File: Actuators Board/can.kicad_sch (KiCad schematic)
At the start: 14 parts, among them U4 SN65HVD230

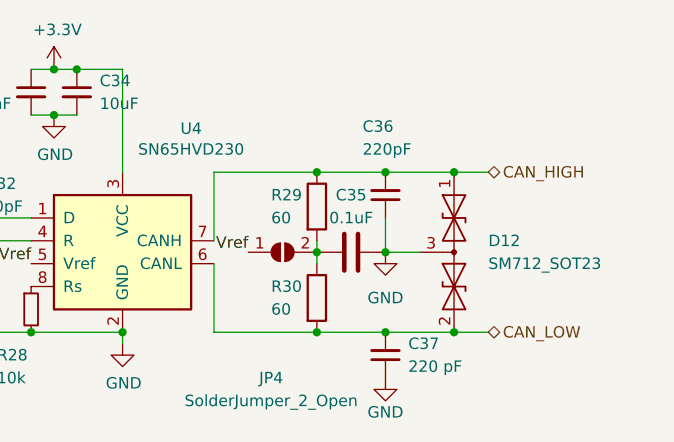
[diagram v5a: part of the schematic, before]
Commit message: Added CAN transceiver and new connector to board
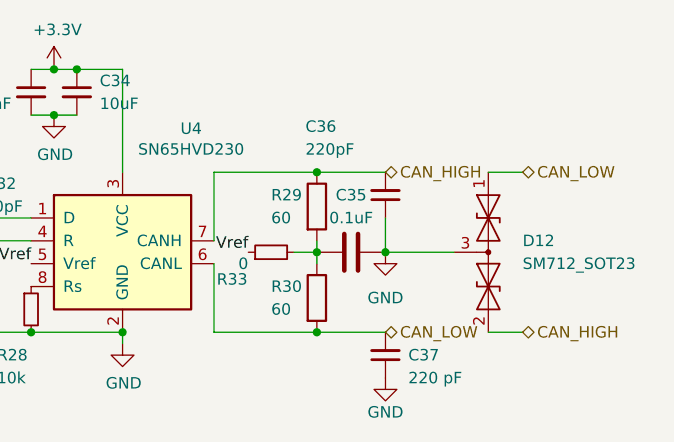
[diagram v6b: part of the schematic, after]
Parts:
- removed JP4: SolderJumper_2_Open, Jumper:SolderJumper-2_P1.3mm_Open_Pad1.0x1.5mm, symbol Jumper:SolderJumper_2_Open
- added R33: 0, Resistor_SMD:R_0603_1608Metric, symbol Device:R_Small
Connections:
- net CAN_HIGH: now also D12.2 (A2); no longer D12.1 (A1)
- net CAN_LOW: now also D12.1 (A1); no longer D12.2 (A2)
- net Vref: now also R33.1
- net at C35.1, R29.2, R30.1: now also R33.2
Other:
- moved on the sheet: D12
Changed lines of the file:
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@@
   (junction (at 163.83 88.9) (diameter 0) (color 0 0 0 0)
   )
-  (junction (at 163.83 97.79) (diameter 0) (color 0 0 0 0)
-  )
   (junction (at 124.46 97.79) (diameter 0) (color 0 0 0 0)
   )
-  (junction (at 171.45 80.01) (diameter 0) (color 0 0 0 0)
-  )
   (junction (at 156.21 97.79) (diameter 0) (color 0 0 0 0)
   )
@@
   (junction (at 134.62 97.79) (diameter 0) (color 0 0 0 0)
   )
-  (junction (at 171.45 97.79) (diameter 0) (color 0 0 0 0)
-  )
-  (junction (at 163.83 80.01) (diameter 0) (color 0 0 0 0)
-  )
   (junction (at 127 73.66) (diameter 0) (color 0 0 0 0)
   )
-  (wire (pts (xy 171.45 97.79) (xy 175.26 97.79))
+  (wire (pts (xy 175.26 97.79) (xy 179.07 97.79))
     (stroke (width 0) (type default) (color 0 0 0 0))
   )
@@
     (stroke (width 0) (type default) (color 0 0 0 0))
   )
-  (wire (pts (xy 163.83 88.9) (xy 167.64 88.9))
+  (wire (pts (xy 163.83 88.9) (xy 171.45 88.9))
     (stroke (width 0) (type default) (color 0 0 0 0))
   )
@@
     (stroke (width 0) (type default) (color 0 0 0 0))
   )
-  (wire (pts (xy 163.83 80.01) (xy 171.45 80.01))
-    (stroke (width 0) (type default) (color 0 0 0 0))
-  )
   (wire (pts (xy 156.21 97.79) (xy 163.83 97.79))
     (stroke (width 0) (type default) (color 0 0 0 0))
@@
     (stroke (width 0) (type default) (color 0 0 0 0))
   )
-  (wire (pts (xy 171.45 80.01) (xy 175.26 80.01))
+  (wire (pts (xy 175.26 80.01) (xy 179.07 80.01))
     (stroke (width 0) (type default) (color 0 0 0 0))
   )
@@
     (stroke (width 0) (type default) (color 0 0 0 0))
   )
-  (wire (pts (xy 163.83 97.79) (xy 171.45 97.79))
-    (stroke (width 0) (type default) (color 0 0 0 0))
-  )
   (wire (pts (xy 134.62 99.06) (xy 134.62 97.79))
     (stroke (width 0) (type default) (color 0 0 0 0))
@@
   )
   (wire (pts (xy 144.78 87.63) (xy 144.78 80.01))
+    (stroke (width 0) (type default) (color 0 0 0 0))
+  )
+  (wire (pts (xy 153.67 88.9) (xy 156.21 88.9))
     (stroke (width 0) (type default) (color 0 0 0 0))
   )
@@
     (effects (font (size 1.27 1.27)) (justify right bottom))
   )
-  (hierarchical_label "CAN_LOW" (shape bidirectional) (at 175.26 97.79 0)
-    (effects (font (size 1.27 1.27)) (justify left))
-  )
   (hierarchical_label "CAN_RX" (shape input) (at 111.76 87.63 180)
     (effects (font (size 1.27 1.27)) (justify right))
   )
+  (hierarchical_label "CAN_HIGH" (shape bidirectional) (at 163.83 80.01 0)
+    (effects (font (size 1.27 1.27)) (justify left))
+  )
   (hierarchical_label "CAN_TX" (shape output) (at 111.76 85.09 180)
     (effects (font (size 1.27 1.27)) (justify right))
   )
-  (hierarchical_label "CAN_HIGH" (shape bidirectional) (at 175.26 80.01 0)
+  (hierarchical_label "CAN_HIGH" (shape bidirectional) (at 179.07 97.79 0)
+    (effects (font (size 1.27 1.27)) (justify left))
+  )
+  (hierarchical_label "CAN_LOW" (shape bidirectional) (at 179.07 80.01 0)
+    (effects (font (size 1.27 1.27)) (justify left))
+  )
+  (hierarchical_label "CAN_LOW" (shape bidirectional) (at 163.83 97.79 0)
     (effects (font (size 1.27 1.27)) (justify left))
   )
@@
     (pin "2")
   )
-  (symbol (lib_id "Jumper:SolderJumper_2_Open") (at 152.4 88.9 0) (unit 1)
-    (in_bom yes) (on_board yes)
-    (property "Reference" "JP4" (id 0) (at 151.13 102.87 0))
-    (property "Value" "SolderJumper_2_Open" (id 1) (at 151.13 105.41 0))
-    (property "Footprint" "Jumper:SolderJumper-2_P1.3mm_Open_Pad1.0x1.5mm" (id 2) (at 152.4 88.9 0)
-      (effects (font (size 1.27 1.27)) hide)
-    )
-    (property "Datasheet" "~" (id 3) (at 152.4 88.9 0)
-      (effects (font (size 1.27 1.27)) hide)
-    )
-    (pin "1")
-    (pin "2")
-  )
   (symbol (lib_id "Device:C_Small") (at 163.83 82.55 180) (unit 1)
     (in_bom yes) (on_board yes)
-    (property "Reference" "C36" (id 0) (at 161.29 74.93 0)
-      (effects (font (size 1.27 1.27)) (justify right))
-    )
-    (property "Value" "220pF" (id 1) (at 161.29 77.47 0)
+    (property "Reference" "C36" (id 0) (at 154.94 74.93 0)
+      (effects (font (size 1.27 1.27)) (justify right))
+    )
+    (property "Value" "220pF" (id 1) (at 154.94 77.47 0)
       (effects (font (size 1.27 1.27)) (justify right))
     )
@@
     (pin "2")
   )
-  (symbol (lib_id "Diode:SM712_SOT23") (at 171.45 88.9 270) (unit 1)
-    (in_bom yes) (on_board yes)
-    (property "Reference" "D12" (id 0) (at 175.26 87.63 90)
-      (effects (font (size 1.27 1.27)) (justify left))
-    )
-    (property "Value" "SM712_SOT23" (id 1) (at 175.26 90.17 90)
-      (effects (font (size 1.27 1.27)) (justify left))
-    )
-    (property "Footprint" "Package_TO_SOT_SMD:SOT-23" (id 2) (at 162.56 88.9 0)
-      (effects (font (size 1.27 1.27)) hide)
-    )
-    (property "Datasheet" "https://www.littelfuse.com/~/media/electronics/datasheets/tvs_diode_arrays/littelfuse_tvs_diode_array_sm712_datasheet.pdf.pdf" (id 3) (at 171.45 85.09 0)
+  (symbol (lib_id "Diode:SM712_SOT23") (at 175.26 88.9 270) (unit 1)
+    (in_bom yes) (on_board yes)
+    (property "Reference" "D12" (id 0) (at 179.07 87.63 90)
+      (effects (font (size 1.27 1.27)) (justify left))
+    )
+    (property "Value" "SM712_SOT23" (id 1) (at 179.07 90.17 90)
+      (effects (font (size 1.27 1.27)) (justify left))
+    )
+    (property "Footprint" "Package_TO_SOT_SMD:SOT-23" (id 2) (at 166.37 88.9 0)
+      (effects (font (size 1.27 1.27)) hide)
+    )
+    (property "Datasheet" "https://www.littelfuse.com/~/media/electronics/datasheets/tvs_diode_arrays/littelfuse_tvs_diode_array_sm712_datasheet.pdf.pdf" (id 3) (at 175.26 85.09 0)
       (effects (font (size 1.27 1.27)) hide)
     )
@@
     (pin "2")
   )
+  (symbol (lib_id "Device:R_Small") (at 151.13 88.9 90) (unit 1)
+    (in_bom yes) (on_board yes)
+    (property "Reference" "R33" (id 0) (at 148.5073 91.9112 90)
+      (effects (font (size 1.27 1.27)) (justify left))
+    )
+    (property "Value" "0" (id 1) (at 148.59 90.17 90)
+      (effects (font (size 1.27 1.27)) (justify left))
+    )
+    (property "Footprint" "Resistor_SMD:R_0603_1608Metric" (id 2) (at 151.13 88.9 0)
+      (effects (font (size 1.27 1.27)) hide)
+    )
+    (property "Datasheet" "~" (id 3) (at 151.13 88.9 0)
+      (effects (font (size 1.27 1.27)) hide)
+    )
+    (pin "1")
+    (pin "2")
+  )
   (symbol (lib_id "Device:R_Small") (at 124.46 95.25 0) (unit 1)
     (in_bom yes) (on_board yes)
@@
   (symbol (lib_id "Device:C_Small") (at 163.83 100.33 180) (unit 1)
     (in_bom yes) (on_board yes)
-    (property "Reference" "C37" (id 0) (at 166.37 99.06 0)
-      (effects (font (size 1.27 1.27)) (justify right))
-    )
-    (property "Value" "220 pF" (id 1) (at 166.37 101.6 0)
-      (effects (font (size 1.27 1.27)) (justify right))
-    )
+    (property "Reference" "C37" (id 0) (at 166.37 100.33 0)
+      (effects (font (size 1.27 1.27)) (justify right))
+    )
+    (property "Value" "220 pF" (id 1) (at 166.37 102.87 0)
+      (effects (font (size 1.27 1.27)) (justify right))
+    )
